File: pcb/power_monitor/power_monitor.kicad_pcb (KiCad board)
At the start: 2 copper layers, 60 x 62 mm, 21 parts, among them J1 230V AC Input, J2 230V AC Output, J3 RFID, J4 OLED, J5 WS2812, K1 G2RL-2A-DC5, Q1 FDN339AN, U1 Wemos-D1-mini, U2 ACS723xMATR-10AB

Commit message: Fixed power-monitor PCB, to match real-life fixes
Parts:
- added R4: 15K, Resistor_SMD:R_0603_1608Metric_Pad1.05x0.95mm_HandSolder, F.Cu at (94.7, 53.2)
- J3: value RFID -> OLED
- J4: value OLED -> RFID
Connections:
- Q1 pad 2: Net-(D1-Pad2) -> GND
- Q1 pad 3: GND -> Net-(D1-Pad2)
- U1 pad 1: (no net) -> Net-(U1-Pad1)
- U1 pad 11: (no net) -> Net-(U1-Pad11)
- U1 pad 12: (no net) -> Net-(U1-Pad12)
- U1 pad 15: (no net) -> Net-(U1-Pad15)
- U1 pad 16: (no net) -> Net-(U1-Pad16)
- U1 pad 3: (no net) -> Net-(U1-Pad3)
- U1 pad 8: (no net) -> +3V3
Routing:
- net RFID_SW: track 40.5 -> 61.3 mm
- net GND: track 139.5 -> 145.6 mm, vias 9 -> 8
- net Net-(D1-Pad2): track 10.1 -> 12.1 mm

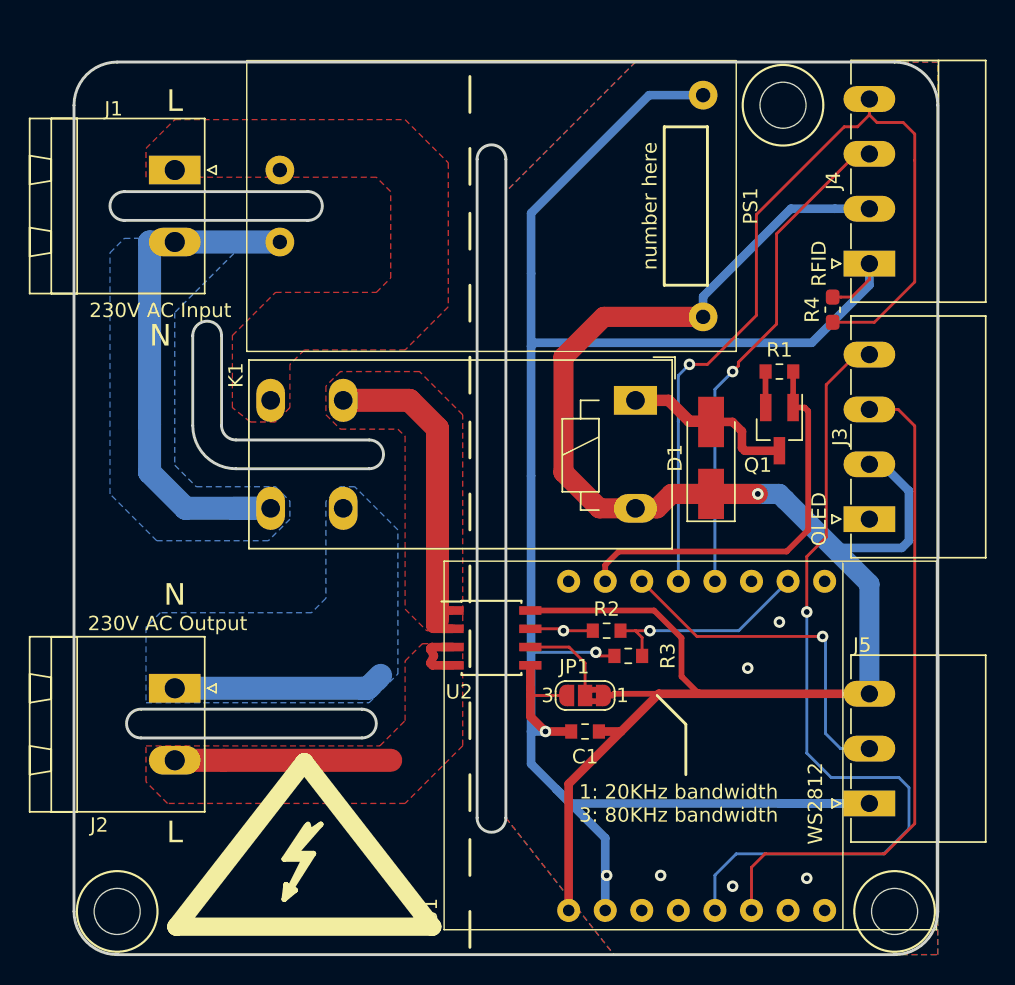
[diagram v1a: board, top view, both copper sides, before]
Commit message: Updated power_monitor pcb to use IRM-02 PSU
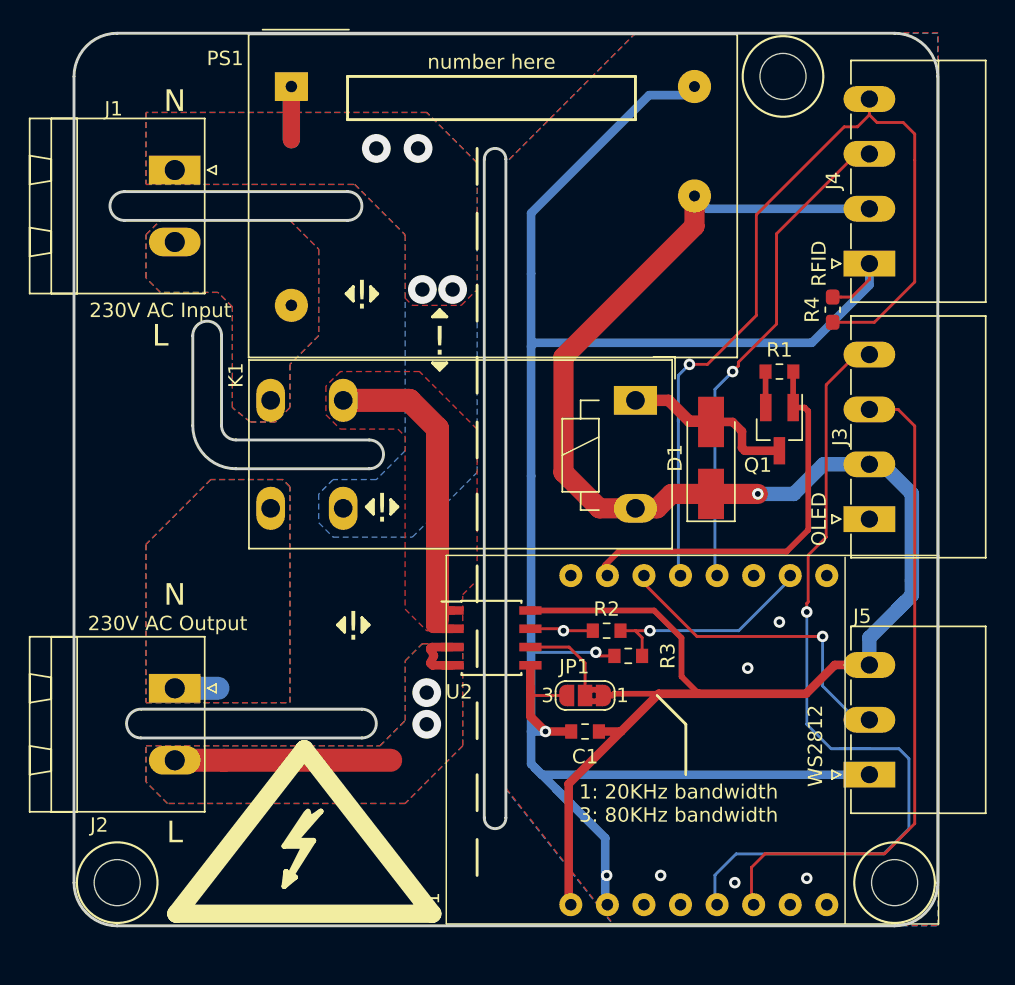
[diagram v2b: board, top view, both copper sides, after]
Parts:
- PS1: value HLK-PM01 -> IRM-02-5; footprint Converter_ACDC:HLK-PM01 -> Converter_ACDC:Converter_ACDC_MeanWell_IRM-02-xx_THT
- moved PS1 16.2 mm to (57.1, 37.7)
- moved J5 2.00 mm to (97.2, 85.5)
- moved REF** 2.00 mm to (45.0, 93.0)
- moved REF** 2.00 mm to (99.0, 93.0)
- moved REF** 2.00 mm to (91.2, 37.0)
- moved REF** 0.90 mm to (58.0, 91.3) (x2)
- moved U1 0.43 mm to (85.4, 83.1)
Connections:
- J1 pad 1: /Power Handling/AC_L -> /Power Handling/AC_N
- J1 pad 2: /Power Handling/AC_N -> /Power Handling/AC_L
- K1 pad 21: /Power Handling/AC_N_Switched -> /Power Handling/AC_N
- K1 pad 24: /Power Handling/AC_N -> /Power Handling/AC_N_Switched
- PS1 pad 1: /Power Handling/AC_L -> /Power Handling/AC_N
- PS1 pad 2: /Power Handling/AC_N -> /Power Handling/AC_L
- U1 pad 1: Net-(U1-Pad1) -> (no net)
- U1 pad 11: Net-(U1-Pad11) -> (no net)
- U1 pad 12: Net-(U1-Pad12) -> (no net)
- U1 pad 15: Net-(U1-Pad15) -> (no net)
- U1 pad 16: Net-(U1-Pad16) -> (no net)
- U1 pad 3: Net-(U1-Pad3) -> (no net)
- U1 pad 8: +3V3 -> (no net)
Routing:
- net /Power Handling/AC_N: track 37.1 -> 7.40 mm, vias 0 -> 4
- net /Power Handling/AC_N_Switched: track 15.7 -> 3.00 mm
- net +5V: track 143.5 -> 134.9 mm
- net GND: track 145.6 -> 142.0 mm
- net WS2812: track 24.5 -> 22.1 mm
- net SDA: track 58.2 -> 60.2 mm
- net /Power Handling/AC_L_Switched: vias 0 -> 2
- added copper zone on B.Cu, net /Power Handling/AC_L
- added copper zone on B.Cu, net /Power Handling/AC_L_Switched
- added copper zone on F.Cu, net /Power Handling/AC_N
- added copper zone on F.Cu, net /Power Handling/AC_N_Switched
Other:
- outline, holes or cut-outs redrawn
- board text added: "!"
- board text added: "! = 230v between points"
- board text added: "<- LV | HV ->"
